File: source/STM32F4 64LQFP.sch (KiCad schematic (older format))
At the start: 16 parts, among them J5 UNUSED MCU PINS, P5 SWD, U5 STM32F405RGT6, X1 8MHz 10ppm (X50328MSB2GI)

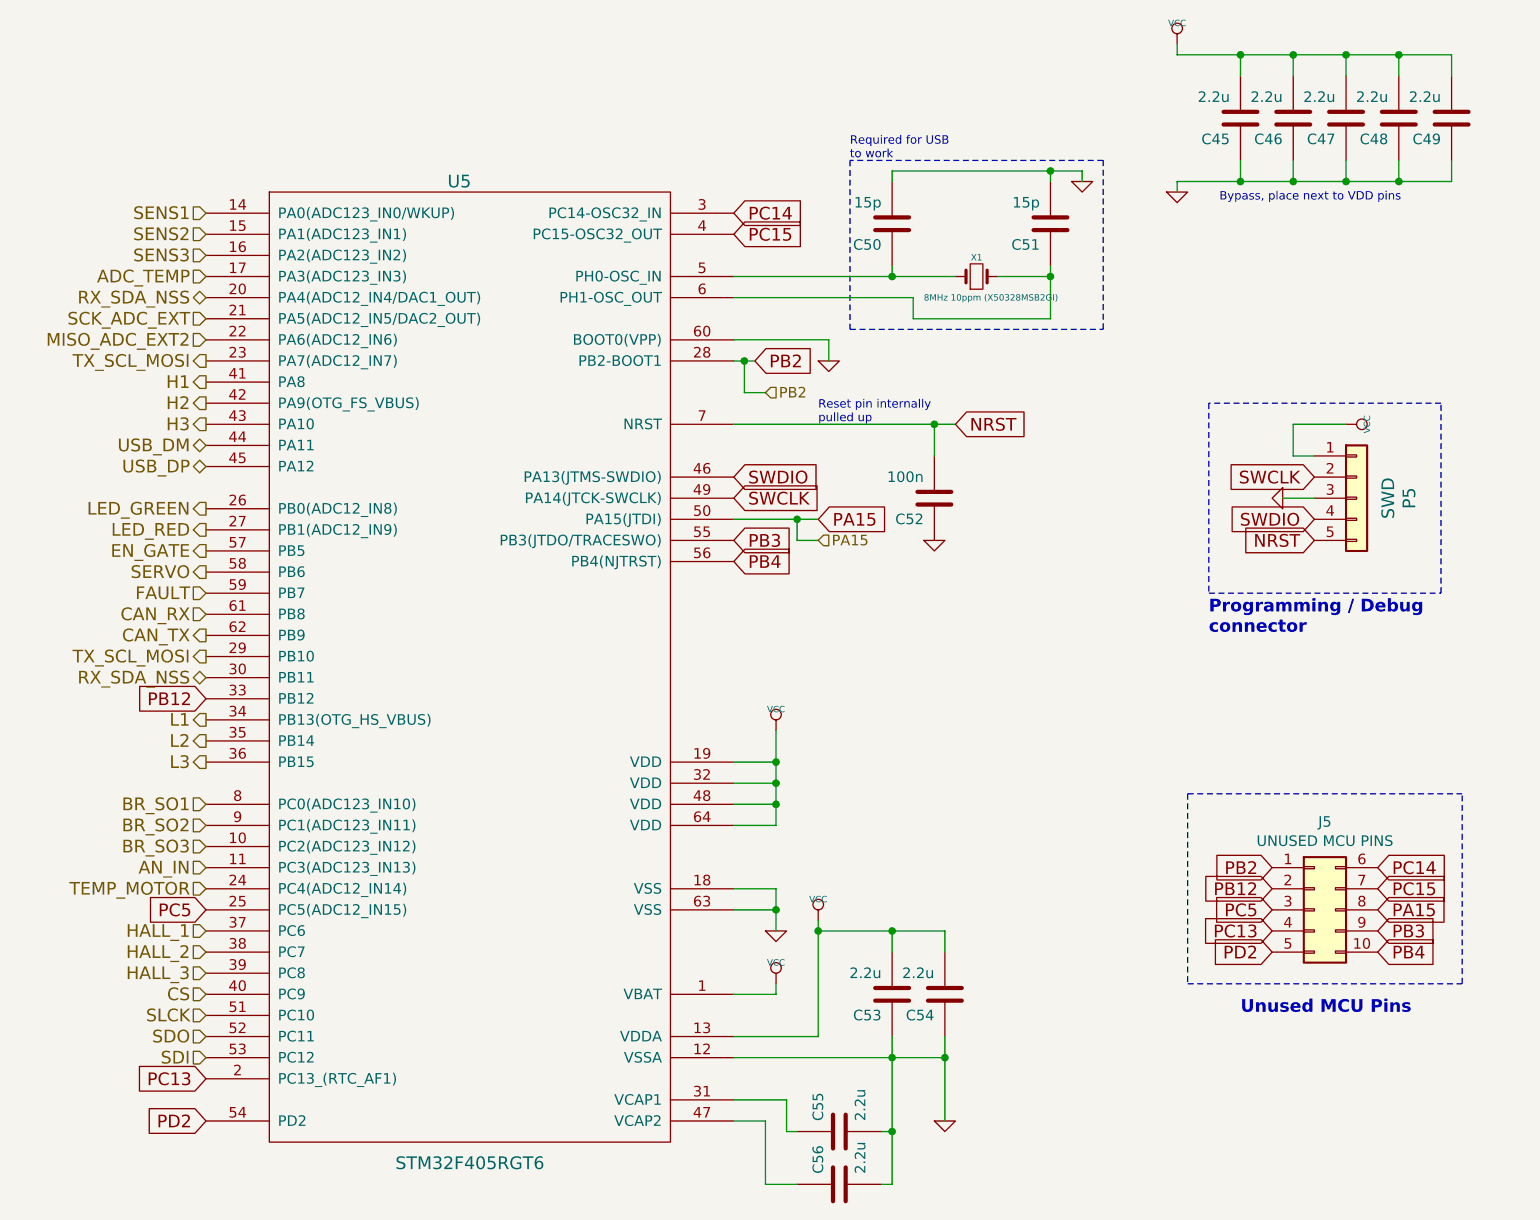
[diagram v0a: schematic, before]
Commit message: started redrawing pcb
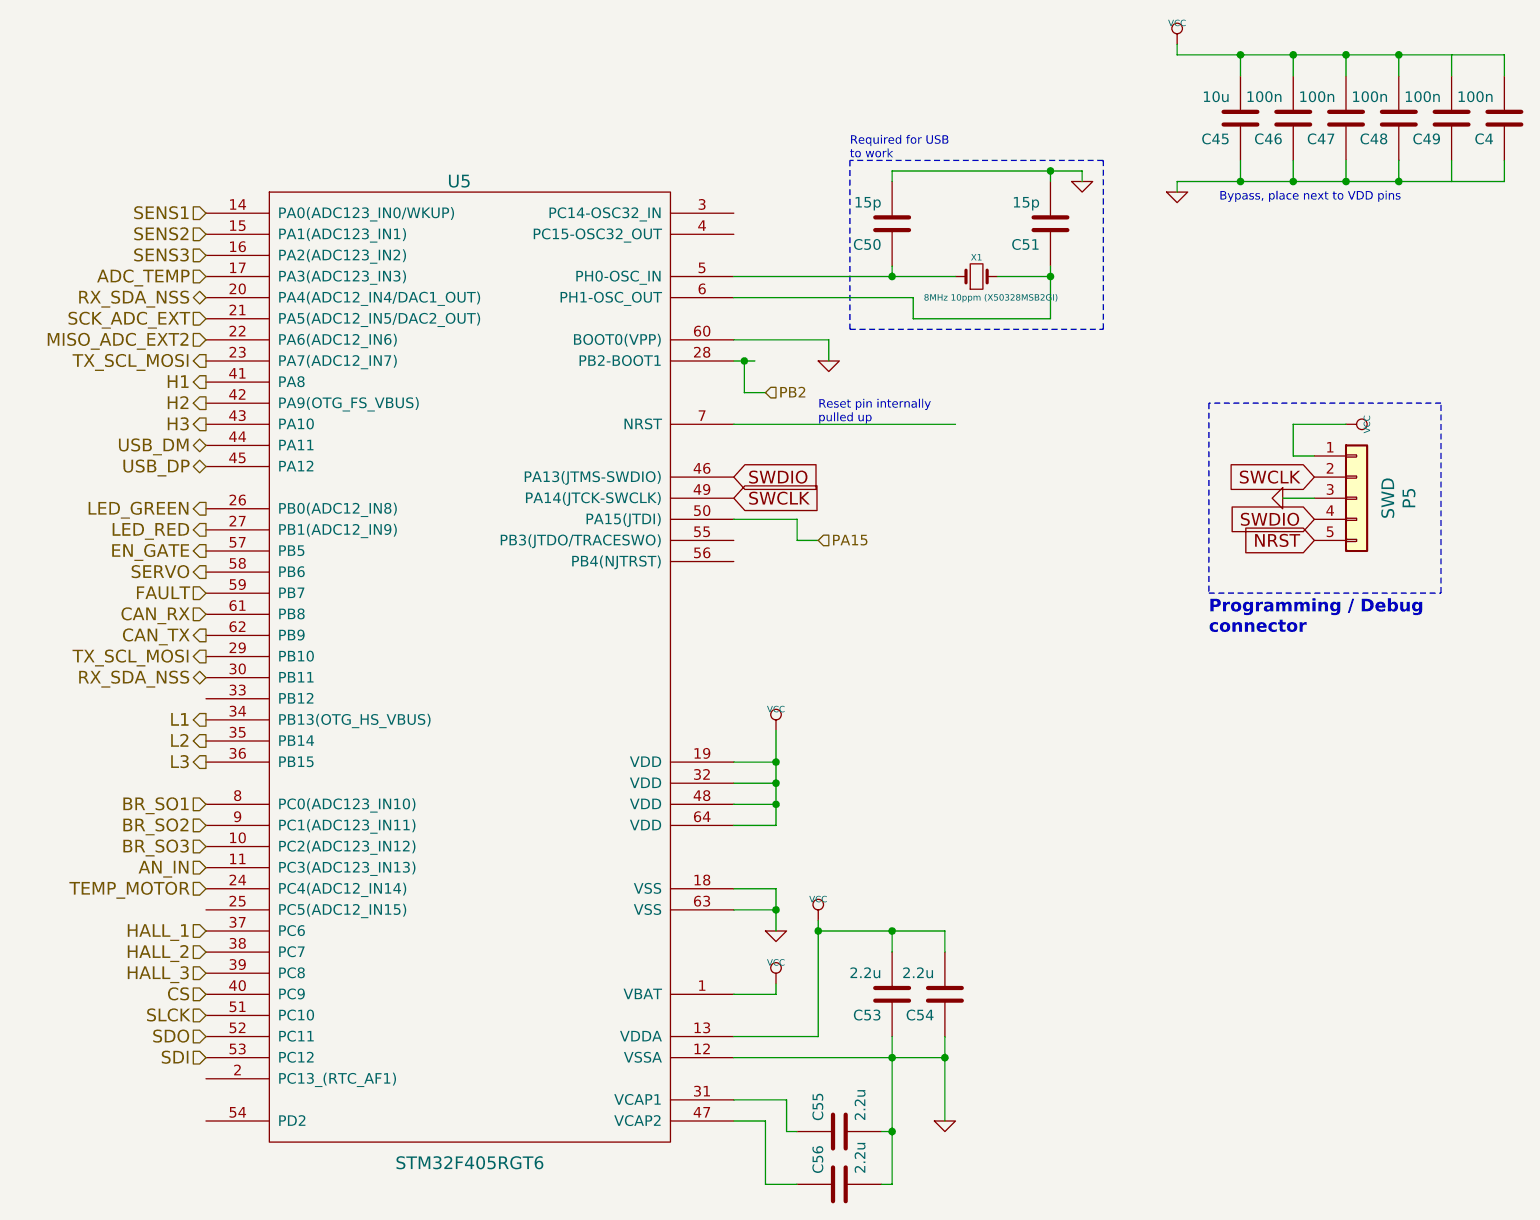
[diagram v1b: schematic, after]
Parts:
- removed C52: 100n, Capacitor_SMD:C_0603_1608Metric, symbol BLDC_4-rescue:C-RESCUE-BLDC_4
- removed J5: UNUSED MCU PINS, Connector_PinHeader_2.00mm:PinHeader_2x05_P2.00mm_Vertical, symbol Connector_Generic:Conn_02x05_Top_Bottom
- added C4: 100n, Capacitor_SMD:C_0402_1005Metric, symbol BLDC_4-rescue:C-RESCUE-BLDC_4
- C45: value 2.2u -> 10u
- C46, C47, C48, C49: value 2.2u -> 100n; footprint Capacitor_SMD:C_0603_1608Metric -> Capacitor_SMD:C_0402_1005Metric
- C50, C51, C53, C54, C55, C56: footprint Capacitor_SMD:C_0603_1608Metric -> Capacitor_SMD:C_0402_1005Metric
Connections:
- net GND: now also C4.1
- net NRST: no longer U5.7 (NRST)
- net VCC: now also C4.2
- net PB12: no longer names the net of U5.33 (PB12)
- net PB3: no longer names the net of U5.55 (PB3(JTDO/TRACESWO))
- net PB4: no longer names the net of U5.56 (PB4(NJTRST))
- net PC13: no longer names the net of U5.2 (PC13_(RTC_AF1))
- net PC14: no longer names the net of U5.3 (PC14-OSC32_IN)
- net PC15: no longer names the net of U5.4 (PC15-OSC32_OUT)
- net PC5: no longer names the net of U5.25 (PC5(ADC12_IN15))
- net PD2: no longer names the net of U5.54 (PD2)
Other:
- note removed: "Unused MCU Pins\n"
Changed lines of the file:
@@
 $Descr A4 11693 8268
 encoding utf-8
-Sheet 6 8
+Sheet 6 6
 Title "Cheap FOCer 2"
 Date "2020-04-08"
@@
 F 0 "C56" H 7550 6450 50  0000 L CNN
 F 1 "2.2u" H 7550 6250 50  0000 L CNN
-F 2 "Capacitor_SMD:C_0603_1608Metric" H 7500 6350 60  0001 C CNN
+F 2 "Capacitor_SMD:C_0402_1005Metric" H 7500 6350 60  0001 C CNN
 F 3 "" H 7500 6350 60  0001 C CNN
 	1    7500 6350
@@
 F 0 "C55" H 7550 6200 50  0000 L CNN
 F 1 "2.2u" H 7550 6000 50  0000 L CNN
-F 2 "Capacitor_SMD:C_0603_1608Metric" H 7500 6100 60  0001 C CNN
+F 2 "Capacitor_SMD:C_0402_1005Metric" H 7500 6100 60  0001 C CNN
 F 3 "" H 7500 6100 60  0001 C CNN
 	1    7500 6100
@@
 F 0 "C50" H 7800 1900 50  0000 L CNN
 F 1 "15p" H 7800 1700 50  0000 L CNN
-F 2 "Capacitor_SMD:C_0603_1608Metric" H 7750 1800 60  0001 C CNN
+F 2 "Capacitor_SMD:C_0402_1005Metric" H 7750 1800 60  0001 C CNN
 F 3 "" H 7750 1800 60  0001 C CNN
 	1    7750 1800
@@
 F 0 "C51" H 8550 1900 50  0000 L CNN
 F 1 "15p" H 8550 1700 50  0000 L CNN
-F 2 "Capacitor_SMD:C_0603_1608Metric" H 8500 1800 60  0001 C CNN
+F 2 "Capacitor_SMD:C_0402_1005Metric" H 8500 1800 60  0001 C CNN
 F 3 "" H 8500 1800 60  0001 C CNN
 	1    8500 1800
@@
 F 0 "C53" H 7800 5550 50  0000 L CNN
 F 1 "2.2u" H 7800 5350 50  0000 L CNN
-F 2 "Capacitor_SMD:C_0603_1608Metric" H 7750 5450 60  0001 C CNN
+F 2 "Capacitor_SMD:C_0402_1005Metric" H 7750 5450 60  0001 C CNN
 F 3 "" H 7750 5450 60  0001 C CNN
 	1    7750 5450
@@
 F 0 "C54" H 8050 5550 50  0000 L CNN
 F 1 "2.2u" H 8050 5350 50  0000 L CNN
-F 2 "Capacitor_SMD:C_0603_1608Metric" H 8000 5450 60  0001 C CNN
+F 2 "Capacitor_SMD:C_0402_1005Metric" H 8000 5450 60  0001 C CNN
 F 3 "" H 8000 5450 60  0001 C CNN
 	1    8000 5450
@@
 	1    0    0    -1
 $EndComp
-$Comp
-L BLDC_4-rescue:GND-RESCUE-BLDC_4 #PWR076
-U 1 1 53F75856
-P 7950 3300
-F 0 "#PWR076" H 7950 3300 30  0001 C CNN
-F 1 "GND" H 7950 3230 30  0001 C CNN
-F 2 "" H 7950 3300 60  0001 C CNN
-F 3 "" H 7950 3300 60  0001 C CNN
-	1    7950 3300
-	1    0    0    -1
-$EndComp
 Wire Wire Line
 	7200 5450 7200 5400
@@
 	7750 6350 7700 6350
 $Comp
-L BLDC_4-rescue:C-RESCUE-BLDC_4 C52
-U 1 1 53F75896
-P 7950 3100
-F 0 "C52" H 8000 3200 50  0000 L CNN
-F 1 "100n" H 8000 3000 50  0000 L CNN
-F 2 "Capacitor_SMD:C_0603_1608Metric" H 7950 3100 60  0001 C CNN
-F 3 "" H 7950 3100 60  0001 C CNN
-	1    7950 3100
-	-1   0    0    1
-$EndComp
-$Comp
 L Connector_Generic:Conn_01x05 P5
 U 1 1 53F77410
@@
 P 9400 1300
 F 0 "C45" H 9450 1400 50  0000 L CNN
-F 1 "2.2u" H 9450 1200 50  0000 L CNN
+F 1 "10u" H 9450 1200 50  0000 L CNN
 F 2 "Capacitor_SMD:C_0603_1608Metric" H 9400 1300 60  0001 C CNN
 F 3 "" H 9400 1300 60  0001 C CNN
@@
 P 9650 1300
 F 0 "C46" H 9700 1400 50  0000 L CNN
-F 1 "2.2u" H 9700 1200 50  0000 L CNN
-F 2 "Capacitor_SMD:C_0603_1608Metric" H 9650 1300 60  0001 C CNN
+F 1 "100n" H 9700 1200 50  0000 L CNN
+F 2 "Capacitor_SMD:C_0402_1005Metric" H 9650 1300 60  0001 C CNN
 F 3 "" H 9650 1300 60  0001 C CNN
 	1    9650 1300
@@
 P 10400 1300
 F 0 "C49" H 10450 1400 50  0000 L CNN
-F 1 "2.2u" H 10450 1200 50  0000 L CNN
-F 2 "Capacitor_SMD:C_0603_1608Metric" H 10400 1300 60  0001 C CNN
+F 1 "100n" H 10450 1200 50  0000 L CNN
+F 2 "Capacitor_SMD:C_0402_1005Metric" H 10400 1300 60  0001 C CNN
 F 3 "" H 10400 1300 60  0001 C CNN
 	1    10400 1300
@@
 P 9900 1300
 F 0 "C47" H 9950 1400 50  0000 L CNN
-F 1 "2.2u" H 9950 1200 50  0000 L CNN
-F 2 "Capacitor_SMD:C_0603_1608Metric" H 9900 1300 60  0001 C CNN
+F 1 "100n" H 9950 1200 50  0000 L CNN
+F 2 "Capacitor_SMD:C_0402_1005Metric" H 9900 1300 60  0001 C CNN
 F 3 "" H 9900 1300 60  0001 C CNN
 	1    9900 1300
@@
 P 10150 1300
 F 0 "C48" H 10200 1400 50  0000 L CNN
-F 1 "2.2u" H 10200 1200 50  0000 L CNN
-F 2 "Capacitor_SMD:C_0603_1608Metric" H 10150 1300 60  0001 C CNN
+F 1 "100n" H 10200 1200 50  0000 L CNN
+F 2 "Capacitor_SMD:C_0402_1005Metric" H 10150 1300 60  0001 C CNN
 F 3 "" H 10150 1300 60  0001 C CNN
 	1    10150 1300
@@
 Wire Notes Line
 	10350 2650 9250 2650
-Wire Wire Line
-	7000 2750 7950 2750
-Wire Wire Line
-	7950 2750 7950 2900
 Text Notes 7400 2750 0    40   ~ 0
 Reset pin internally\npulled up
-Text GLabel 8050 2750 2    60   Input ~ 0
-NRST
 Text Notes 7550 1500 0    40   ~ 0
 Required for USB\nto work
@@
 SDO
 Wire Wire Line
-	7950 2750 8050 2750
-Connection ~ 7950 2750
-Text GLabel 7400 3200 2    60   Input ~ 0
-PA15
-Text GLabel 7000 3300 2    60   Input ~ 0
-PB3
-Text GLabel 7000 3400 2    60   Input ~ 0
-PB4
-Text GLabel 7100 2450 2    60   Input ~ 0
-PB2
-Wire Wire Line
 	7000 2350 7450 2350
 Wire Wire Line
@@
 Wire Wire Line
 	7000 2150 7850 2150
-Text GLabel 7000 1750 2    60   Input ~ 0
-PC14
-Text GLabel 7000 1850 2    60   Input ~ 0
-PC15
-Text GLabel 4500 4050 0    60   Input ~ 0
-PB12
-Text GLabel 4500 5050 0    60   Input ~ 0
-PC5
 $Comp
 L BLDC_4-rescue:STM32F40X_LQFP64 U5
@@
 	1    0    0    -1
 $EndComp
-Text GLabel 4500 5850 0    60   Input ~ 0
-PC13
-Text GLabel 4500 6050 0    60   Input ~ 0
-PD2
-$Comp
-L Connector_Generic:Conn_02x05_Top_Bottom J5
-U 1 1 5D71EE29
-P 9750 5050
-F 0 "J5" H 9800 5467 50  0000 C CNN
-F 1 "UNUSED MCU PINS" H 9800 5376 50  0000 C CNN
-F 2 "Connector_PinHeader_2.00mm:PinHeader_2x05_P2.00mm_Vertical" H 9750 5050 50  0001 C CNN
-F 3 "~" H 9750 5050 50  0001 C CNN
-	1    9750 5050
-	1    0    0    -1
-$EndComp
-Text GLabel 10050 5050 2    60   Input ~ 0
-PA15
-Text GLabel 10050 5150 2    60   Input ~ 0
-PB3
-Text GLabel 10050 5250 2    60   Input ~ 0
-PB4
-Text GLabel 10050 4850 2    60   Input ~ 0
-PC14
-Text GLabel 10050 4950 2    60   Input ~ 0
-PC15
-Text GLabel 9550 5150 0    60   Input ~ 0
-PC13
-Text GLabel 9550 5250 0    60   Input ~ 0
-PD2
-Text GLabel 9550 5050 0    60   Input ~ 0
-PC5
-Text GLabel 9550 4950 0    60   Input ~ 0
-PB12
-Text GLabel 9550 4850 0    60   Input ~ 0
-PB2
-Wire Notes Line
-	9150 4500 9150 5400
-Wire Notes Line
-	10450 5400 10450 4500
-Wire Notes Line
-	9150 5400 10450 5400
-Wire Notes Line
-	9150 4500 10450 4500
 Wire Wire Line
 	7750 2050 8050 2050
@@
 	8250 2050 8500 2050
 Wire Wire Line
-	7400 3200 7300 3200
-Wire Wire Line
 	7300 3300 7300 3200
-Connection ~ 7300 3200
 Wire Wire Line
 	7300 3200 7000 3200
 Text Notes 9250 3750 0    60   ~ 12
 Programming / Debug\nconnector
-Text Notes 9400 5550 0    60   ~ 12
-Unused MCU Pins\n
 Wire Wire Line
 	7400 3300 7300 3300
@@
 Text HLabel 7150 2600 2    50   Input ~ 0
 PB2
+$Comp
+L BLDC_4-rescue:C-RESCUE-BLDC_4 C4
+U 1 1 5EE0476E
+P 10650 1300
+F 0 "C4" H 10700 1400 50  0000 L CNN
+F 1 "100n" H 10700 1200 50  0000 L CNN
+F 2 "Capacitor_SMD:C_0402_1005Metric" H 10650 1300 60  0001 C CNN
+F 3 "" H 10650 1300 60  0001 C CNN
+	1    10650 1300
+	-1   0    0    1
+$EndComp
+Wire Wire Line
+	10650 1000 10650 1100
+Wire Wire Line
+	10650 1600 10650 1500
+Wire Wire Line
+	10400 1600 10650 1600
+Wire Wire Line
+	10400 1000 10650 1000
+Wire Wire Line
+	7000 2750 8050 2750
 $EndSCHEMATC
